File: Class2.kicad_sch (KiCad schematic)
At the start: 36 parts, among them J1 USB_C_Receptacle, J2 Conn_01x02_Pin, J3 Conn_ARM_JTAG_SWD_10, U1 STM32G030F6P6, U2 LR4054, U3 TPS613222ADBZ, U4 AMS1117-3.3, U5 MCP601R, U6 MCP4017-xxxxLT

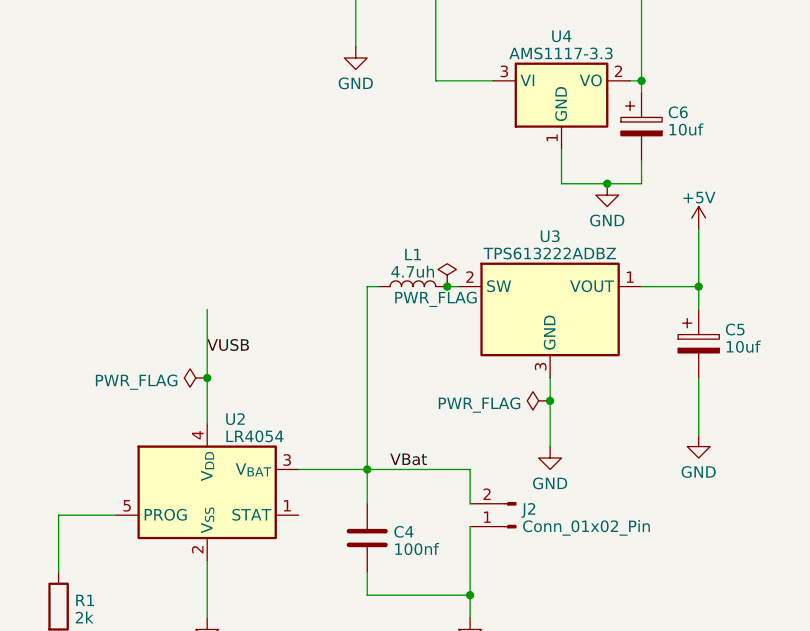
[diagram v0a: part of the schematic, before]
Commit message: add power switch, cleanups
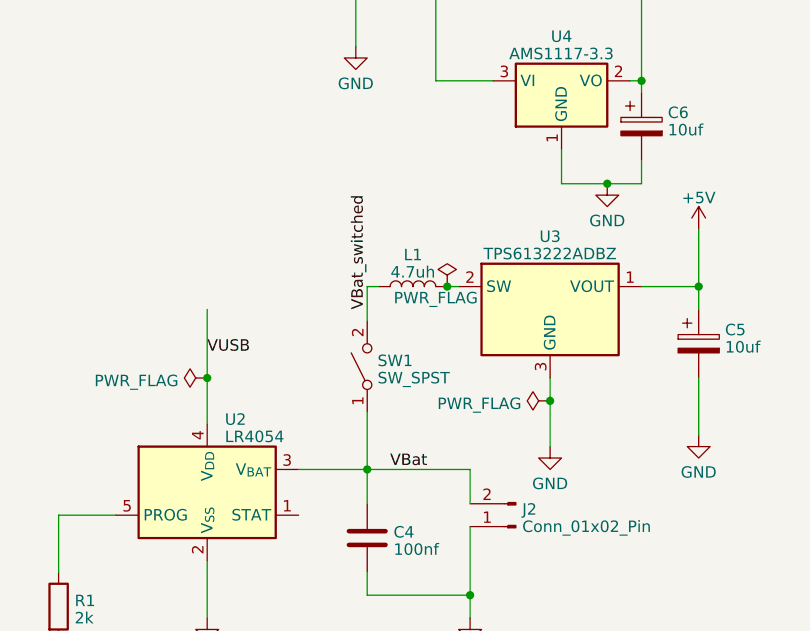
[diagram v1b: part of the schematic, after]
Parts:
- added SW1: SW_SPST, Button_Switch_SMD:SW_SPDT_CK-JS102011SAQN, symbol Switch:SW_SPST
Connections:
- net VBat: now also SW1.1 (A); no longer L1.1
- new net VBat_switched: L1.1, SW1.2 (B)
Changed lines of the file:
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@@
+    (stroke (width 0) (type default))
+  )
+  (wire (pts (xy 57.15 149.86) (xy 57.15 156.21))
     (stroke (width 0) (type default))
   )
@@
     (stroke (width 0) (type default))
   )
-  (wire (pts (xy 57.15 135.89) (xy 57.15 156.21))
-    (stroke (width 0) (type default))
-  )
   (wire (pts (xy 182.88 91.44) (xy 189.23 91.44))
     (stroke (width 0) (type default))
@@
     (stroke (width 0) (type default))
   )
+  (wire (pts (xy 57.15 135.89) (xy 57.15 139.7))
+    (stroke (width 0) (type default))
+  )
   (wire (pts (xy 77.47 146.05) (xy 77.47 148.59))
     (stroke (width 0) (type default))
@@
   )
   (label "trans" (at 80.01 77.47 0) (fields_autoplaced)
+    (effects (font (size 1.27 1.27)) (justify left bottom))
+  )
+  (label "VBat_switched" (at 57.15 138.43 90) (fields_autoplaced)
     (effects (font (size 1.27 1.27)) (justify left bottom))
   )
@@
         )
       )
+    )
+  )
+  (symbol (lib_id "Switch:SW_SPST") (at 57.15 144.78 90) (unit 1)
+    (in_bom yes) (on_board yes) (dnp no) (fields_autoplaced)
+    (property "Reference" "SW1" (at 58.293 144.1363 90)
+      (effects (font (size 1.27 1.27)) (justify right))
+    )
+    (property "Value" "SW_SPST" (at 58.293 146.0573 90)
+      (effects (font (size 1.27 1.27)) (justify right))
+    )
+    (property "Footprint" "Button_Switch_SMD:SW_SPDT_CK-JS102011SAQN" (at 57.15 144.78 0)
+      (effects (font (size 1.27 1.27)) hide)
+    )
+    (property "Datasheet" "~" (at 57.15 144.78 0)
+      (effects (font (size 1.27 1.27)) hide)
+    )
+    (pin "1")
+    (pin "2")
+    (instances
+      (project "Class2"
+        (path "/b0f42d21-78ce-41e8-b624-34371c0ceb55"
+          (reference "SW1") (unit 1)
+        )
+      )

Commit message: update board to use instrumentation amp
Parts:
- removed R6: 510k, Resistor_SMD:R_0603_1608Metric, symbol Device:R
- removed U5: MCP601R, Package_TO_SOT_SMD:SOT-23-5, symbol Amplifier_Operational:MCP601R
- added U5: INA350, Package_SON:Texas_DQK, symbol Amplifier_Instrumentation:INA350
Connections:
- net +3V3: now also U5.7 (V+)
- net GND: now also U5.4 (V-)
- net trans: now also U5.6
- net at R3.2, R4.1: now also R5.1, U6.6 (W), U5.2 (-), U5.3 (+)
- net Gain Select: now reaches U1.12 (PA5)
- net Gain Select: now also U5.1 (Gain_Select)

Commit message: production
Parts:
- removed R3, R4: ~, Sensor:strain_gauge, symbol Sensor:strain_gauge
- removed R5: 9k1, Resistor_SMD:R_0603_1608Metric, symbol Device:R
- removed U5: INA350, Package_SON:Texas_DQK, symbol Amplifier_Instrumentation:INA350
- removed U6: MCP4017-xxxxLT, Package_TO_SOT_SMD:SOT-363_SC-70-6, symbol Potentiometer_Digital:MCP4017-xxxxLT
- C5, C6: LCSC (none) -> C249450; LCSC Part (none) -> C249450
- C7, C8: LCSC (none) -> C249551; LCSC Part (none) -> C249551
- D1, D10, D11, D12, D2, D3, D4, D5, D6, D7, D8, D9: LCSC (none) -> C114586; LCSC Part (none) -> C114586
- J1: footprint Connector_USB:USB_C_Receptacle_GCT_USB4135-GF-A_6P_TopMnt_Horizontal -> Connector_USB:USB_C_Receptacle_HRO_TYPE-C-31-M-12; LCSC Part (none) -> C165948
- J2: LCSC (none) -> C173752; LCSC Part (none) -> C173752
- J3: LCSC (none) -> C180221; LCSC Part (none) -> C180221
- L1: footprint Inductor_SMD:L_Murata_DFE201610P -> Inductor_SMD:L_Vishay_IHLP-2020; LCSC Part (none) -> C845007
- SW1: LCSC Part (none) -> C221660
- U1: MPN (none) -> C724040
- U2: LCSC Part (none) -> C5336483
- U3: value TPS613222ADBZ -> TPS613222ADBV; footprint Package_TO_SOT_SMD:SOT-23 -> Package_TO_SOT_SMD:SOT-23-5; symbol Regulator_Switching:TPS613222ADBZ -> Regulator_Switching:TPS613222ADBV; LCSC Part (none) -> C2071163
- U4: LCSC Part (none) -> C2904742
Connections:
- net +5V: now also U3.4 (VOUT); no longer U3.1 (VOUT)
- net GND: now also U3.2 (GND); no longer U3.3 (GND)
- net at L1.2: now also U3.1 (SW); no longer U3.2 (SW)

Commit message: fix drc and erc
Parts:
- added D13: SD103, Diode_SMD:D_SOD-323F, symbol Device:D_Schottky
- J3: LCSC C180221 -> C5160761; LCSC Part C180221 -> C5160761
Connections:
- net +5V: now also D13.1 (K)
- net VUSB: now also D13.2 (A)
- no-connect marks 0 -> 32
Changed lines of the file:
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@@
   (junction (at 270.51 91.44) (diameter 0) (color 0 0 0 0)
   )
+  (junction (at 93.98 133.35) (diameter 0) (color 0 0 0 0)
+  )
   (junction (at 157.48 71.12) (diameter 0) (color 0 0 0 0)
   )
@@
   (junction (at 241.3 29.21) (diameter 0) (color 0 0 0 0)
   )
+  (no_connect (at 83.82 69.85))
+  (no_connect (at 49.53 161.29))
+  (no_connect (at 76.2 62.23))
+  (no_connect (at 254 43.18))
+  (no_connect (at 35.56 72.39))
+  (no_connect (at 83.82 67.31))
+  (no_connect (at 76.2 57.15))
+  (no_connect (at 135.89 156.21))
+  (no_connect (at 135.89 171.45))
+  (no_connect (at 35.56 62.23))
+  (no_connect (at 135.89 148.59))
+  (no_connect (at 35.56 59.69))
+  (no_connect (at 35.56 69.85))
+  (no_connect (at 135.89 146.05))
+  (no_connect (at 83.82 72.39))
+  (no_connect (at 135.89 153.67))
+  (no_connect (at 76.2 64.77))
+  (no_connect (at 135.89 140.97))
+  (no_connect (at 135.89 135.89))
+  (no_connect (at 76.2 74.93))
+  (no_connect (at 135.89 176.53))
+  (no_connect (at 129.54 76.2))
+  (no_connect (at 135.89 161.29))
+  (no_connect (at 76.2 54.61))
+  (no_connect (at 135.89 133.35))
+  (no_connect (at 135.89 168.91))
+  (no_connect (at 87.63 77.47))
+  (no_connect (at 135.89 163.83))
+  (no_connect (at 135.89 138.43))
+  (no_connect (at 135.89 179.07))
+  (no_connect (at 129.54 78.74))
+  (no_connect (at 76.2 59.69))
   (wire (pts (xy 204.47 91.44) (xy 213.36 91.44))
     (stroke (width 0) (type default))
@@
     (stroke (width 0) (type default))
   )
+  (wire (pts (xy 93.98 133.35) (xy 93.98 135.89))
+    (stroke (width 0) (type default))
+  )
   (wire (pts (xy 226.06 41.91) (xy 226.06 43.18))
     (stroke (width 0) (type default))
@@
     (stroke (width 0) (type default))
   )
-  (wire (pts (xy 168.91 170.18) (xy 168.91 175.26))
-    (stroke (width 0) (type default))
-  )
   (wire (pts (xy 157.48 91.44) (xy 162.56 91.44))
     (stroke (width 0) (type default))
@@
     (stroke (width 0) (type default))
   )
-  (wire (pts (xy 93.98 129.54) (xy 93.98 135.89))
+  (wire (pts (xy 93.98 129.54) (xy 93.98 133.35))
     (stroke (width 0) (type default))
   )
@@
     (stroke (width 0) (type default))
   )
+  (wire (pts (xy 106.68 125.73) (xy 106.68 133.35))
+    (stroke (width 0) (type default))
+  )
   (wire (pts (xy 261.62 50.8) (xy 270.51 50.8))
     (stroke (width 0) (type default))
@@
     (stroke (width 0) (type default))
   )
+  (wire (pts (xy 93.98 133.35) (xy 96.52 133.35))
+    (stroke (width 0) (type default))
+  )
   (wire (pts (xy 182.88 50.8) (xy 189.23 50.8))
     (stroke (width 0) (type default))
   )
+  (wire (pts (xy 104.14 133.35) (xy 106.68 133.35))
+    (stroke (width 0) (type default))
+  )
   (wire (pts (xy 193.04 39.37) (xy 198.12 39.37))
     (stroke (width 0) (type default))
@@
     (stroke (width 0) (type default))
   )
-  (wire (pts (xy 171.45 170.18) (xy 171.45 175.26))
-    (stroke (width 0) (type default))
-  )
   (wire (pts (xy 115.57 93.98) (xy 116.84 93.98))
     (stroke (width 0) (type default))
@@
     (stroke (width 0) (type default))
   )
-  (label "sda" (at 171.45 173.99 90) (fields_autoplaced)
-    (effects (font (size 1.27 1.27)) (justify left bottom))
-  )
   (label "SWDIO" (at 130.81 73.66 0) (fields_autoplaced)
     (effects (font (size 1.27 1.27)) (justify left bottom))
@@
   )
   (label "SWCLK" (at 130.81 71.12 0) (fields_autoplaced)
-    (effects (font (size 1.27 1.27)) (justify left bottom))
-  )
-  (label "scl" (at 168.91 173.99 90) (fields_autoplaced)
     (effects (font (size 1.27 1.27)) (justify left bottom))
   )
@@
   )
   (label "SWDIO" (at 81.28 80.01 0) (fields_autoplaced)
+    (effects (font (size 1.27 1.27)) (justify left bottom))
+  )
+  (label "VUSB" (at 106.68 128.27 0) (fields_autoplaced)
     (effects (font (size 1.27 1.27)) (justify left bottom))
   )
@@
       (effects (font (size 1.27 1.27)) hide)
     )
-    (property "LCSC Part" "C180221" (at 116.84 73.66 0)
+    (property "LCSC Part" "C5160761" (at 116.84 73.66 0)
       (effects (font (size 1.27 1.27)) hide)
     )
@@
       (effects (font (size 1.27 1.27)) hide)
     )
-    (property "LCSC" "C180221" (at 116.84 73.66 0)
+    (property "LCSC" "C5160761" (at 116.84 73.66 0)
       (effects (font (size 1.27 1.27)) hide)
     )
@@
         )
       )
+    )
+  )
+  (symbol (lib_id "Device:D_Schottky") (at 100.33 133.35 0) (unit 1)
+    (in_bom yes) (on_board yes) (dnp no) (fields_autoplaced)
+    (property "Reference" "D13" (at 100.0125 129.0701 0)
+      (effects (font (size 1.27 1.27)))
+    )
+    (property "Value" "SD103" (at 100.0125 130.9911 0)
+      (effects (font (size 1.27 1.27)))
+    )
+    (property "Footprint" "Diode_SMD:D_SOD-323F" (at 100.33 133.35 0)
+      (effects (font (size 1.27 1.27)) hide)
+    )
+    (property "Datasheet" "~" (at 100.33 133.35 0)
+      (effects (font (size 1.27 1.27)) hide)
+    )
+    (pin "1")
+    (pin "2")
+    (instances
+      (project "Class2"
+        (path "/b0f42d21-78ce-41e8-b624-34371c0ceb55"
+          (reference "D13") (unit 1)
+        )
+      )
